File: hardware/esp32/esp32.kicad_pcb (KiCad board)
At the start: 4 copper layers, 50 x 50 mm, 59 parts, among them J1 Screw_Terminal_01x02, Q1 MMBT5401, Q2 MMBT2222A, U2 LMV321, U3 LMV321, U4 mini_esp32, U5 HT7533-1, U6 LM393

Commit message: Work on V3.1
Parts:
- added J2: ESP_left, Library:PinHeader_2x10_P2.54mm_Vertical, F.Cu at (114.3, 80.3)
- added J3: ESP_right, Library:PinHeader_2x10_P2.54mm_Vertical, F.Cu at (139.7, 80.3)
- added R33: 47k, Library:R_0603_1608Metric_Pad0.98x0.95mm_HandSolder, F.Cu at (156.5, 100.1)
- R22: value 10k -> 4k7
- R6: value 18k -> 47k
- R8: value 47k -> 10k
- U4: footprint Library:ESP32_mini -> Library:ESP32_mini_no_pads
- moved C1 0.51 mm to (153.2, 106.4)
- moved R2 0.36 mm to (156.0, 105.4)
- turned R22 to -90 degrees
- turned R6 to 0 degrees
- turned R8 to 180 degrees
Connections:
- C7 pad 1: +3.3V -> +5V
- R17 pad 1: +3.3V -> +5V
- R18 pad 2: +3.3V -> +5V
- R22 pad 1: Net-(C10-Pad2) -> /GIRA_TX
- R22 pad 2: /GIRA_TX -> Net-(C10-Pad2)
- R6 pad 1: GND -> Net-(U1--)
- R6 pad 2: Net-(U1--) -> GND
- R8 pad 1: Net-(Q2-C) -> Net-(Q1-B1)
- R8 pad 2: Net-(Q1-B1) -> Net-(Q2-C)
- U3 pad 5: +3.3V -> +5V
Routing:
- net +5V: track 26.6 -> 34.3 mm, vias 5 -> 10
- net +3.3V: track 29.6 -> 24.0 mm, vias 14 -> 10
- net GND: track 38.0 -> 32.7 mm, vias 46 -> 53
- net Net-(U1--): track 4.55 -> 5.96 mm
- net /GIRA_RX_COMP: track 21.1 -> 22.3 mm
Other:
- board text added: "Door Bus"
- board text added: "max. 40Vdc"
- board text removed: "Bus"

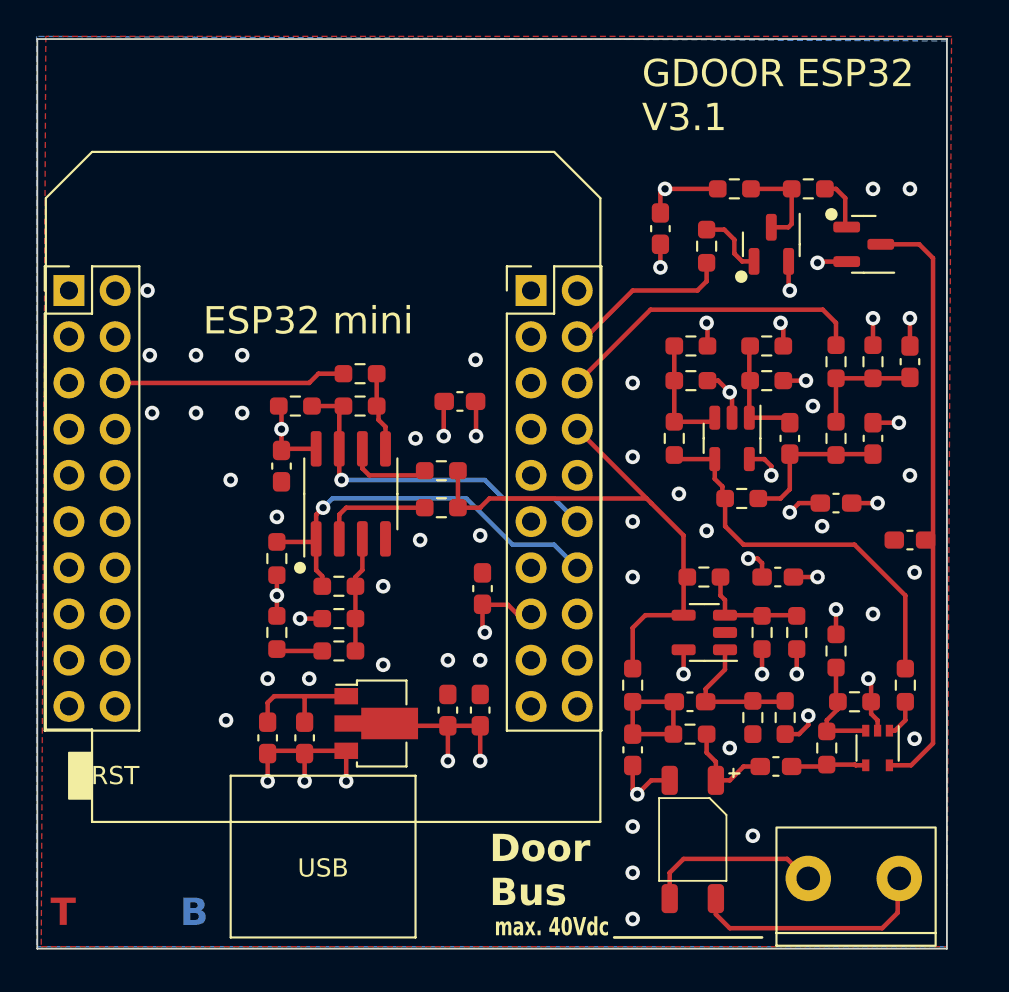
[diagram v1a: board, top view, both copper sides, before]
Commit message: Mark boot pins and move rx pins to non boot pins
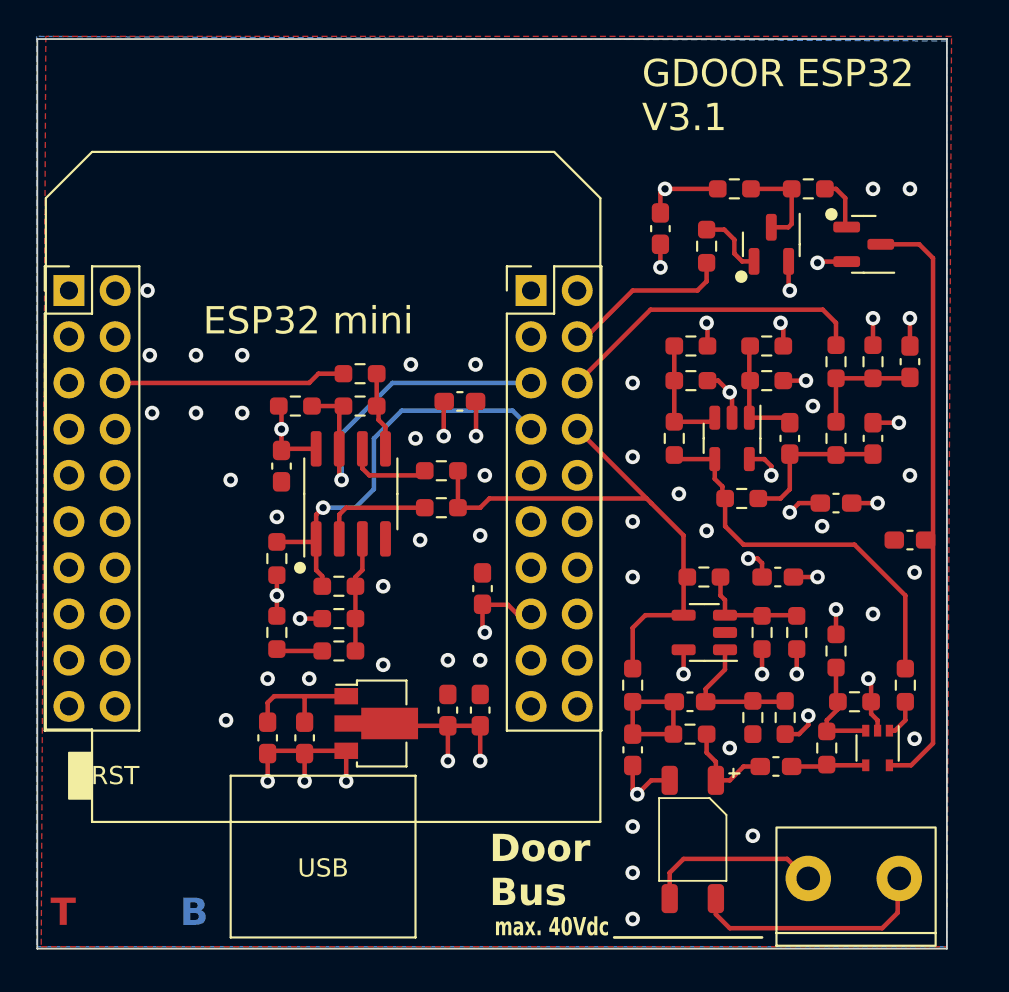
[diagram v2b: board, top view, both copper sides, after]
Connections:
- J3 pad 12: /GIRA_RX_DAC -> unconnected-(J3-IO_04-Pad12)
- J3 pad 14: /GIRA_RX_COMP -> unconnected-(J3-IO_00-Pad14)
- J3 pad 5: unconnected-(J3-IO_22/D1/SCL-Pad5) -> /GIRA_RX_DAC
- J3 pad 7: unconnected-(J3-IO_21/D2/SDA-Pad7) -> /GIRA_RX_COMP
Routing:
- net GND: vias 53 -> 55
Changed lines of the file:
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@@
   (net 51 "unconnected-(J3-TXD-Pad1)")
   (net 52 "unconnected-(J3-RXD-Pad3)")
-  (net 53 "unconnected-(J3-IO_22{slash}D1{slash}SCL-Pad5)")
-  (net 54 "unconnected-(J3-IO_21{slash}D2{slash}SDA-Pad7)")
+  (net 53 "unconnected-(J3-IO_04-Pad12)")
+  (net 54 "unconnected-(J3-IO_00-Pad14)")
   (net 55 "unconnected-(J3-IO_17{slash}D3-Pad9)")
   (net 56 "unconnected-(J3-IO_16{slash}D4-Pad11)")
@@
       (net 22 "/GIRA_TX_EN") (pinfunction "IO_27") (pintype "passive"))
     (pad "5" thru_hole oval (at 0 5.08) (size 1.7 1.7) (drill 1) (layers "*.Cu" "*.Mask")
-      (net 53 "unconnected-(J3-IO_22{slash}D1{slash}SCL-Pad5)") (pinfunction "IO_22/D1/SCL") (pintype "passive+no_connect"))
+      (net 30 "/GIRA_RX_DAC") (pinfunction "IO_22/D1/SCL") (pintype "passive"))
     (pad "6" thru_hole oval (at 2.54 5.08) (size 1.7 1.7) (drill 1) (layers "*.Cu" "*.Mask")
       (net 24 "/GIRA_TX") (pinfunction "IO_25") (pintype "passive"))
     (pad "7" thru_hole oval (at 0 7.62) (size 1.7 1.7) (drill 1) (layers "*.Cu" "*.Mask")
-      (net 54 "unconnected-(J3-IO_21{slash}D2{slash}SDA-Pad7)") (pinfunction "IO_21/D2/SDA") (pintype "passive+no_connect"))
+      (net 29 "/GIRA_RX_COMP") (pinfunction "IO_21/D2/SDA") (pintype "passive"))
     (pad "8" thru_hole oval (at 2.54 7.62) (size 1.7 1.7) (drill 1) (layers "*.Cu" "*.Mask")
       (net 19 "/GIRA_RX") (pinfunction "IO_32") (pintype "passive"))
@@
       (net 56 "unconnected-(J3-IO_16{slash}D4-Pad11)") (pinfunction "IO_16/D4") (pintype "passive+no_connect"))
     (pad "12" thru_hole oval (at 2.54 12.7) (size 1.7 1.7) (drill 1) (layers "*.Cu" "*.Mask")
-      (net 30 "/GIRA_RX_DAC") (pinfunction "IO_04") (pintype "passive"))
+      (net 53 "unconnected-(J3-IO_04-Pad12)") (pinfunction "IO_04") (pintype "passive+no_connect"))
     (pad "13" thru_hole oval (at 0 15.24) (size 1.7 1.7) (drill 1) (layers "*.Cu" "*.Mask")
       (net 3 "GND") (pinfunction "GND") (pintype "passive"))
     (pad "14" thru_hole oval (at 2.54 15.24) (size 1.7 1.7) (drill 1) (layers "*.Cu" "*.Mask")
-      (net 29 "/GIRA_RX_COMP") (pinfunction "IO_00") (pintype "passive"))
+      (net 54 "unconnected-(J3-IO_00-Pad14)") (pinfunction "IO_00") (pintype "passive+no_connect"))
     (pad "15" thru_hole oval (at 0 17.78) (size 1.7 1.7) (drill 1) (layers "*.Cu" "*.Mask")
       (net 7 "+5V") (pinfunction "VCC_(USB)") (pintype "passive"))
@@
   )
   (segment (start 155.8525 106.426) (end 155.956 106.3225) (width 0.25) (layer "F.Cu") (net 1))
-  (segment (start 158.1 106.36) (end 157.546 106.36) (width 0.25) (layer "F.Cu") (net 1))
   (segment (start 154.0245 106.426) (end 155.8525 106.426) (width 0.25) (layer "F.Cu") (net 1))
-  (segment (start 157.5085 106.3225) (end 155.956 106.3225) (width 0.25) (layer "F.Cu") (net 1))
-  (segment (start 157.546 106.36) (end 157.5085 106.3225) (width 0.25) (layer "F.Cu") (net 1))
+  (segment (start 158.1 106.36) (end 155.9935 106.36) (width 0.25) (layer "F.Cu") (net 1))
+  (segment (start 155.9935 106.36) (end 155.956 106.3225) (width 0.25) (layer "F.Cu") (net 1))
   (segment (start 151.384 106.426) (end 152.2995 106.426) (width 0.25) (layer "F.Cu") (net 2))
   (segment (start 149.86 107.188) (end 150.622 107.188) (width 0.25) (layer "F.Cu") (net 2))
@@
   (via (at 160.782 104.902) (size 0.8) (drill 0.4) (layers "F.Cu" "B.Cu") (free) (net 3))
   (via (at 158.496 81.788) (size 0.8) (drill 0.4) (layers "F.Cu" "B.Cu") (net 3))
-  (via (at 136.652 84.074) (size 0.8) (drill 0.4) (layers "F.Cu" "B.Cu") (free) (net 3))
+  (via (at 136.652 84.328) (size 0.8) (drill 0.4) (layers "F.Cu" "B.Cu") (free) (net 3))
   (via (at 123.825 86.995) (size 0.8) (drill 0.4) (layers "F.Cu" "B.Cu") (free) (net 3))
   (via (at 131.572 96.52) (size 0.8) (drill 0.4) (layers "F.Cu" "B.Cu") (free) (net 3))
@@
   (via (at 150.622 105.41) (size 0.8) (drill 0.4) (layers "F.Cu" "B.Cu") (net 3))
   (via (at 136.6785 88.265) (size 0.8) (drill 0.4) (layers "F.Cu" "B.Cu") (net 3))
+  (via (at 137.16 90.424) (size 0.8) (drill 0.4) (layers "F.Cu" "B.Cu") (free) (net 3))
   (via (at 145.288 96.012) (size 0.8) (drill 0.4) (layers "F.Cu" "B.Cu") (free) (net 3))
   (via (at 153.924 80.264) (size 0.8) (drill 0.4) (layers "F.Cu" "B.Cu") (net 3))
@@
   (via (at 160.782 95.758) (size 0.8) (drill 0.4) (layers "F.Cu" "B.Cu") (free) (net 3))
   (via (at 158.242 101.6) (size 0.8) (drill 0.4) (layers "F.Cu" "B.Cu") (net 3))
+  (via (at 133.096 84.328) (size 0.8) (drill 0.4) (layers "F.Cu" "B.Cu") (free) (net 3))
   (via (at 121.285 83.82) (size 0.8) (drill 0.4) (layers "F.Cu" "B.Cu") (free) (net 3))
   (via (at 145.288 114.808) (size 0.8) (drill 0.4) (layers "F.Cu" "B.Cu") (free) (net 3))
@@
   (segment (start 128.223 95.965) (end 127.889 95.631) (width 0.25) (layer "F.Cu") (net 29))
   (via (at 128.27 92.202) (size 0.8) (drill 0.4) (layers "F.Cu" "B.Cu") (net 29))
-  (segment (start 136.144 91.694) (end 138.684 94.234) (width 0.25) (layer "B.Cu") (net 29))
-  (segment (start 140.97 94.234) (end 142.24 95.504) (width 0.25) (layer "B.Cu") (net 29))
-  (segment (start 128.27 92.202) (end 128.778 91.694) (width 0.25) (layer "B.Cu") (net 29))
-  (segment (start 138.684 94.234) (end 140.97 94.234) (width 0.25) (layer "B.Cu") (net 29))
-  (segment (start 128.778 91.694) (end 136.144 91.694) (width 0.25) (layer "B.Cu") (net 29))
+  (segment (start 138.684 86.868) (end 139.7 87.884) (width 0.25) (layer "B.Cu") (net 29))
+  (segment (start 131.064 91.186) (end 131.064 88.392) (width 0.25) (layer "B.Cu") (net 29))
+  (segment (start 131.064 88.392) (end 132.588 86.868) (width 0.25) (layer "B.Cu") (net 29))
+  (segment (start 128.27 92.202) (end 130.048 92.202) (width 0.25) (layer "B.Cu") (net 29))
+  (segment (start 130.048 92.202) (end 131.064 91.186) (width 0.25) (layer "B.Cu") (net 29))
+  (segment (start 132.588 86.868) (end 138.684 86.868) (width 0.25) (layer "B.Cu") (net 29))
   (segment (start 129.3895 86.614) (end 127.6585 86.614) (width 0.25) (layer "F.Cu") (net 30))
   (segment (start 129.159 90.551) (end 129.286 90.678) (width 0.25) (layer "F.Cu") (net 30))
@@
   (segment (start 129.159 88.965) (end 129.159 86.8445) (width 0.25) (layer "F.Cu") (net 30))
   (via (at 129.286 90.678) (size 0.8) (drill 0.4) (layers "F.Cu" "B.Cu") (net 30))
-  (segment (start 129.286 90.678) (end 137.16 90.678) (width 0.25) (layer "B.Cu") (net 30))
-  (segment (start 140.97 91.694) (end 142.24 92.964) (width 0.25) (layer "B.Cu") (net 30))
-  (segment (start 138.176 91.694) (end 140.97 91.694) (width 0.25) (layer "B.Cu") (net 30))
-  (segment (start 137.16 90.678) (end 138.176 91.694) (width 0.25) (layer "B.Cu") (net 30))
+  (segment (start 129.286 88.138) (end 132.08 85.344) (width 0.25) (layer "B.Cu") (net 30))
+  (segment (start 132.08 85.344) (end 139.7 85.344) (width 0.25) (layer "B.Cu") (net 30))
+  (segment (start 129.286 90.678) (end 129.286 88.138) (width 0.25) (layer "B.Cu") (net 30))
   (segment (start 131.318 86.7175) (end 131.2145 86.614) (width 0.25) (layer "F.Cu") (net 31))
   (segment (start 131.2145 86.614) (end 131.2145 84.836) (width 0.25) (layer "F.Cu") (net 31))

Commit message: Working on V3.1
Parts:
- removed R22: 4k7, Library:R_0603_1608Metric_Pad0.98x0.95mm_HandSolder
- added C18: 100p, Library:C_0603_1608Metric_Pad1.08x0.95mm_HandSolder, F.Cu at (161.0, 98.6)
- added R34: 0, Library:R_0603_1608Metric_Pad0.98x0.95mm_HandSolder, F.Cu at (156.5, 84.2)
- R14: value 2k4 -> 1k
- R2: value 10k -> 22k
- R33, R6: value 47k -> 18k
- moved C3 9.16 mm to (161.0, 103.1), turned to 90 degrees
- moved R11 3.55 mm to (159.3, 98.6)
- turned R2 to 90 degrees
- turned R33 to -90 degrees
- turned R6 to 180 degrees
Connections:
- net /GIRA_RX renamed /RX_ANA
- net /GIRA_RX_COMP renamed /RX
- net /GIRA_RX_DAC renamed /RX_DAC
- net /GIRA_RX_THRES renamed /DAC_OUT
- net /GIRA_TX_EN renamed /TX_EN
- C3 pad 1: Net-(Q1-C1) -> /5V_onoff
- C7 pad 1: +5V -> /5V_onoff
- J3 pad 6: /GIRA_TX -> /TX
- Q1 pad 3: Net-(Q1-C1) -> /5V_onoff
- R17 pad 1: +5V -> /5V_onoff
- R18 pad 2: +5V -> /5V_onoff
- R2 pad 1: Net-(U1--) -> Net-(C1-Pad1)
- R2 pad 2: Net-(C1-Pad1) -> Net-(U1--)
- R33 pad 1: Net-(U1--) -> /5V_onoff
- R33 pad 2: +5V -> Net-(U1--)
- R6 pad 1: Net-(U1--) -> GND
- R6 pad 2: GND -> Net-(U1--)
- U pad 5: Net-(Q1-C1) -> /5V_onoff
- U3 pad 5: +5V -> /5V_onoff
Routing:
- net Net-(Q1-C1): track 32.8 -> 0.00 mm
- net /TX: track 0.00 -> 17.4 mm
- net /GIRA_TX: track 17.4 -> 0.00 mm
- net /5V_onoff: track 0.00 -> 12.8 mm, vias 0 -> 7
- net +5V: track 34.3 -> 26.6 mm, vias 10 -> 5
- net Net-(R11-Pad1): track 21.7 -> 16.8 mm
- net Net-(U1-+): track 2.13 -> 6.59 mm
- net /RX_ANA: track 30.9 -> 27.7 mm
- added copper zone on In2.Cu, net /5V_onoff
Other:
- board text added: "*Debug Pins"
- board text added: "5Vin"
- board text added: "5Vin: max. 6V, 100mA"
- board text added: "ADC: RX_ANA* (0-3.3V)"
- board text added: "Bus A"
- board text added: "Bus B"
- board text added: "DAC: DAC_OUT* (0-3.3V)"
- board text added: "DAC_OUT"
- board text added: "GND"
- board text added: "GPIO in: RX, RX_DAC*"
- board text added: "GPIO out: TX, TX_EN"
- board text added: "GPIO: CMOS, 3.3V"
- board text added: "RX"
- board text added: "RX_ANA"
- board text added: "RX_DAC"
- board text added: "TX"
- board text added: "TX_EN"

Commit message: Add logo
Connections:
- net /DAC_OUT renamed /RX_THRESH
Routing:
- net GND: track 32.7 -> 32.8 mm, vias 55 -> 54
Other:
- board text added: "*) Debug Pins"
- board text added: "Analog in: RX_THRESH* (0-3.3V)"
- board text added: "Analog out: RX_ANA* (0-3.3V)"
- board text added: "ESP32 V3.1"
- board text added: "GPIO in: TX, TX_EN"
- board text added: "GPIO out: RX, RX_DAC*"
- board text added: "RX_THRESH"
- board text added: "https://github.com/gdoor-org/gdoor"
- board text removed: "*Debug Pins"
- board text removed: "ADC: RX_ANA* (0-3.3V)"
- board text removed: "DAC: DAC_OUT* (0-3.3V)"
- board text removed: "DAC_OUT"
- board text removed: "GDOOR ESP32 V3.1"
- board text removed: "GPIO in: RX, RX_DAC*"
- board text removed: "GPIO out: TX, TX_EN"
